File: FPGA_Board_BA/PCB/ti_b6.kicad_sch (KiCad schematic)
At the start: 1 part, among them U901 BOOSTXL-3PHGANINV

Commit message: schematic almost ready pt2
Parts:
- removed U901: BOOSTXL-3PHGANINV, MYLIB_Misc:TI_BOOSTXL_3PH, symbol MYLIB_Misc:TI_BOOSTXL_3Ph
- added U1001: BOOSTXL-3PHGANINV, MYLIB_Misc:TI_BOOSTXL_3PH, symbol MYLIB_Misc:TI_BOOSTXL_3Ph
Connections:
- net B6_En: now also U1001.13 (En)
- net GND: now also U1001.20 (GND), U1001.22 (GND)
- net I_A: now also U1001.27 (IA)
- net I_B: now also U1001.28 (IB)
- net I_C: now also U1001.29 (IC)
- net OT: now also U1001.34 (OT)
- net PWM_AH: now also U1001.40 (PWM_AH)
- net PWM_AL: now also U1001.39 (PWM_AL)
- net PWM_BH: now also U1001.38 (PWM_BH)
- net PWM_BL: now also U1001.37 (PWM_BL)
- net PWM_CH: now also U1001.36 (PWM_CH)
- net PWM_CL: now also U1001.35 (PWM_CL)
- net V_A: now also U1001.24 (VA)
- net V_B: now also U1001.25 (VB)
- net V_C: now also U1001.26 (VC)
- net V_DC: now also U1001.23 (VDC)
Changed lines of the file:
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@@
+	)
+	(symbol
+		(lib_id "MYLIB_Misc:TI_BOOSTXL_3Ph")
+		(at 187.96 68.58 0)
+		(unit 1)
+		(exclude_from_sim no)
+		(in_bom yes)
+		(on_board yes)
+		(dnp no)
+		(fields_autoplaced yes)
+		(property "Reference" "U1001"
+			(at 187.96 49.53 0)
+			(effects
+				(font
+					(size 1.27 1.27)
+				)
+			)
+		)
+		(property "Value" "BOOSTXL-3PHGANINV"
+			(at 187.96 52.07 0)
+			(effects
+				(font
+					(size 1.27 1.27)
+				)
+			)
+		)
+		(property "Footprint" "MYLIB_Misc:TI_BOOSTXL_3PH"
+			(at 188.976 46.482 0)
+			(effects
+				(font
+					(size 1.27 1.27)
+				)
+				(hide yes)
+			)
+		)
+		(property "Datasheet" "https://www.ti.com/tool/de-de/BOOSTXL-3PHGANINV#tech-docs"
+			(at 188.214 41.656 0)
+			(effects
+				(font
+					(size 1.27 1.27)
+				)
+				(hide yes)
+			)
+		)
+		(property "Description" "48-V-Dreiphasen-Inverter mit Shunt-basierter Inline-Motor Phasen-Strommessung – Evaluierungsmodul"
+			(at 188.214 44.196 0)
+			(effects
+				(font
+					(size 1.27 1.27)
+				)
+				(hide yes)
+			)
+		)
+		(property "Mouser nr Connector" "855-M20-7811045R "
+			(at 188.722 39.37 0)
+			(effects
+				(font
+					(size 1.27 1.27)
+				)
+				(hide yes)
+			)
+		)
+		(pin "20"
+		)
+		(pin "39"
+		)
+		(pin "37"
+		)
+		(pin "38"
+		)
+		(pin "13"
+		)
+		(pin "40"
+		)
+		(pin "26"
+		)
+		(pin "36"
+		)
+		(pin "34"
+		)
+		(pin "35"
+		)
+		(pin "24"
+		)
+		(pin "25"
+		)
+		(pin "22"
+		)
+		(pin "29"
+		)
+		(pin "30"
+		)
+		(pin "27"
+		)
+		(pin "28"
+		)
+		(pin "23"
+		)
+		(instances
+			(project ""
+				(path "/fd7503bc-e7fc-4766-b224-3d1c3d7de5ff/cdd0bf2b-f478-4dc3-9571-56b5ccfa9f0c"
+					(reference "U1001")
+					(unit 1)
+				)
+			)
+		)
 	)
 	(symbol
@@
 					(unit 1)
 				)
-			)
-		)
-	)
-	(symbol
-		(lib_id "MYLIB_Misc:TI_BOOSTXL_3Ph")
-		(at 187.96 68.58 0)
-		(unit 1)
-		(exclude_from_sim no)
-		(in_bom yes)
-		(on_board yes)
-		(dnp no)
-		(fields_autoplaced yes)
-		(property "Reference" "U901"
-			(at 187.96 49.53 0)
-			(effects
-				(font
-					(size 1.27 1.27)
-				)
-			)
-		)
-		(property "Value" "BOOSTXL-3PHGANINV"
-			(at 187.96 52.07 0)
-			(effects
-				(font
-					(size 1.27 1.27)
-				)
-			)
-		)
-		(property "Footprint" "MYLIB_Misc:TI_BOOSTXL_3PH"
-			(at 188.976 46.482 0)
-			(effects
-				(font
-					(size 1.27 1.27)
-				)
-				(hide yes)
-			)
-		)
-		(property "Datasheet" "https://www.ti.com/tool/de-de/BOOSTXL-3PHGANINV#tech-docs"
-			(at 188.214 41.656 0)
-			(effects
-				(font
-					(size 1.27 1.27)
-				)
-				(hide yes)
-			)
-		)
-		(property "Description" "48-V-Dreiphasen-Inverter mit Shunt-basierter Inline-Motor Phasen-Strommessung – Evaluierungsmodul"
-			(at 188.214 44.196 0)
-			(effects
-				(font
-					(size 1.27 1.27)
-				)
-				(hide yes)
-			)
-		)
-		(pin "22"
-		)
-		(pin "24"
-		)
-		(pin "34"
-		)
-		(pin "28"
-		)
-		(pin "13"
-		)
-		(pin "29"
-		)
-		(pin "23"
-		)
-		(pin "30"
-		)
-		(pin "27"
-		)
-		(pin "20"
-		)
-		(pin "36"
-		)
-		(pin "37"
-		)
-		(pin "38"
-		)
-		(pin "39"
-		)
-		(pin "40"
-		)
-		(pin "35"
-		)
-		(pin "26"
-		)
-		(pin "25"
-		)
-		(instances
-			(project ""
-				(path "/fd7503bc-e7fc-4766-b224-3d1c3d7de5ff/cdd0bf2b-f478-4dc3-9571-56b5ccfa9f0c"
-					(reference "U901")
-					(unit 1)
-				)

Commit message: lots of work
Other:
- note added: "All pins scaled to max 3.3V"
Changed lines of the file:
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@@
 	(generator_version "9.0")
 	(paper "A4")
+	(text "All pins scaled to max 3.3V"
+		(exclude_from_sim no)
+		(at 40.64 113.538 0)
+		(effects
+			(font
+				(size 1.27 1.27)
+			)
+		)
+	)
 	(no_connect
 		(at 175.26 77.47)

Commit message: work
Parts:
- renumbered U1001 to U14
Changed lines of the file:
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@@
 		(dnp no)
 		(fields_autoplaced yes)
-		(property "Reference" "U1001"
+		(property "Reference" "U14"
 			(at 187.96 49.53 0)
 			(effects
@@
 			(project ""
 				(path "/fd7503bc-e7fc-4766-b224-3d1c3d7de5ff/cdd0bf2b-f478-4dc3-9571-56b5ccfa9f0c"
-					(reference "U1001")
+					(reference "U14")
 					(unit 1)
 				)
@@
 		(dnp no)
 		(fields_autoplaced yes)
-		(property "Reference" "#PWR0901"
+		(property "Reference" "#PWR067"
 			(at 167.64 90.17 0)
 			(effects
@@
 			(project ""
 				(path "/fd7503bc-e7fc-4766-b224-3d1c3d7de5ff/cdd0bf2b-f478-4dc3-9571-56b5ccfa9f0c"
-					(reference "#PWR0901")
+					(reference "#PWR067")
 					(unit 1)
 				)

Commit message: 22.11
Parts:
- renumbered U14 to U10
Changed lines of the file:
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@@
 		(dnp no)
 		(fields_autoplaced yes)
-		(property "Reference" "U14"
+		(property "Reference" "U10"
 			(at 187.96 49.53 0)
 			(effects
@@
 			(project ""
 				(path "/fd7503bc-e7fc-4766-b224-3d1c3d7de5ff/cdd0bf2b-f478-4dc3-9571-56b5ccfa9f0c"
-					(reference "U14")
+					(reference "U10")
 					(unit 1)
 				)
@@
 		(dnp no)
 		(fields_autoplaced yes)
-		(property "Reference" "#PWR067"
+		(property "Reference" "#PWR074"
 			(at 167.64 90.17 0)
 			(effects
@@
 			(project ""
 				(path "/fd7503bc-e7fc-4766-b224-3d1c3d7de5ff/cdd0bf2b-f478-4dc3-9571-56b5ccfa9f0c"
-					(reference "#PWR067")
+					(reference "#PWR074")
 					(unit 1)
 				)

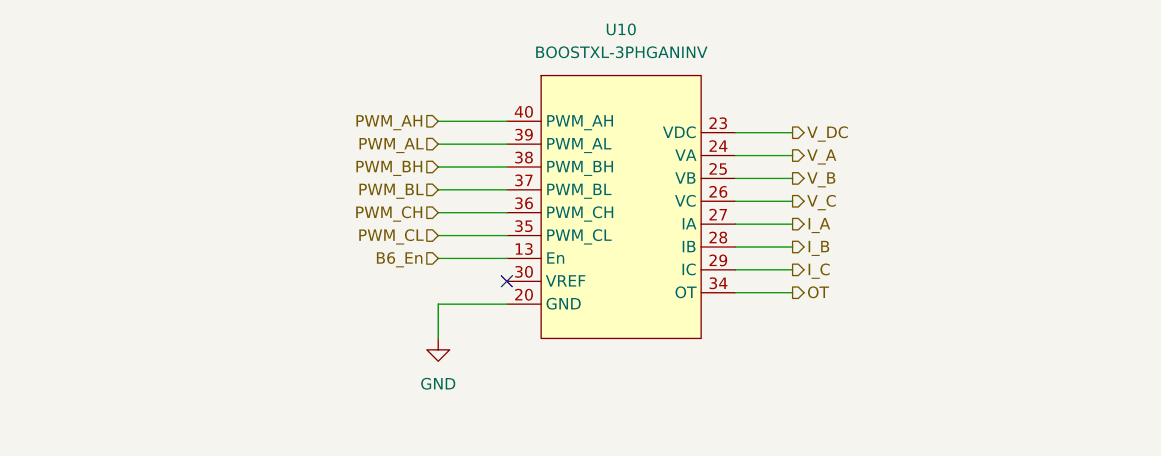
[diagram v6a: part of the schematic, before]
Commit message: big schematic cleanup. Added wire to bus
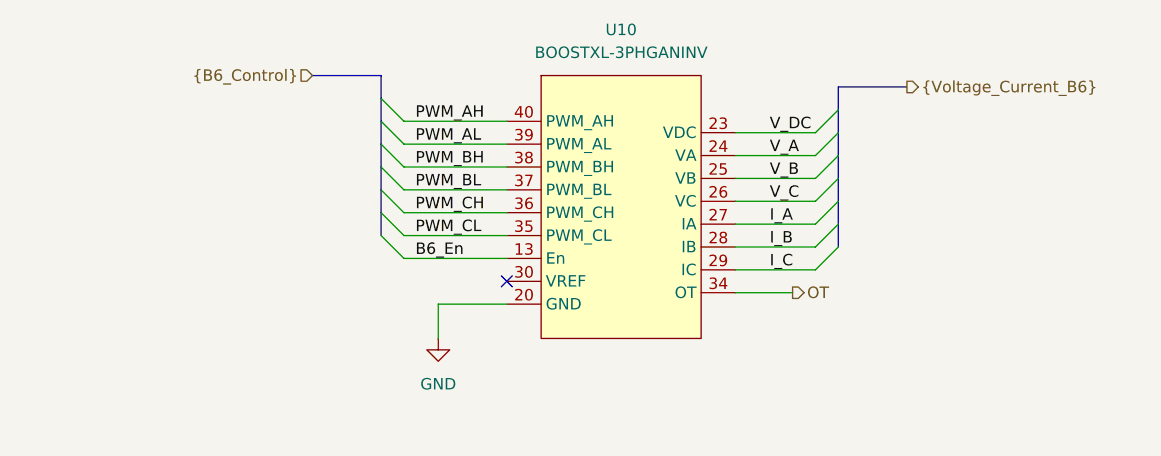
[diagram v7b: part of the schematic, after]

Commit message: PCB left side almost finished + some optimization in schematics
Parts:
- U10: Mouser nr Connector 855-M20-7811045R -> 710-61002021121
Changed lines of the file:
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@@
 	(generator_version "9.0")
 	(paper "A4")
+	(bus_alias "B6_Control"
+		(members "PWM_AH" "PWM_AL" "PWM_BH" "PWM_BL" "PWM_CH" "PWM_CL" "B6_En")
+	)
 	(text "All pins scaled to max 3.3V"
 		(exclude_from_sim no)
@@
 			)
 		)
-		(property "Mouser nr Connector" "855-M20-7811045R "
+		(property "Mouser nr Connector" "710-61002021121"
 			(at 188.722 39.37 0)
 			(effects
